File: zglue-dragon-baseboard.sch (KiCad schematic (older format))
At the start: 1 part

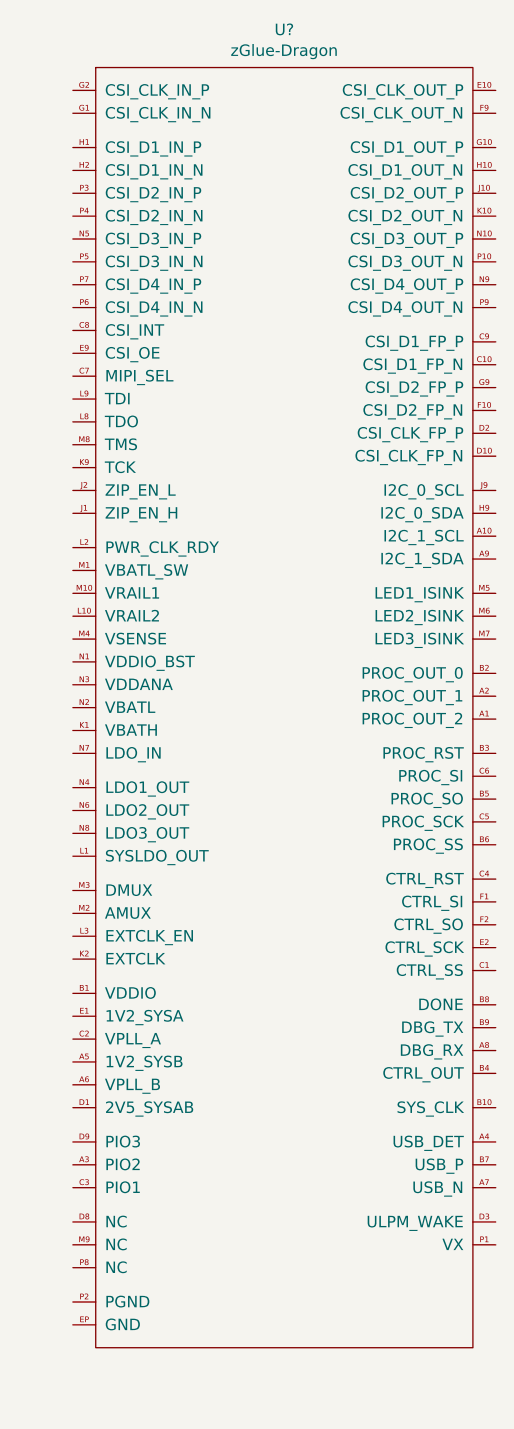
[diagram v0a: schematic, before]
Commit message: Added .gitignore
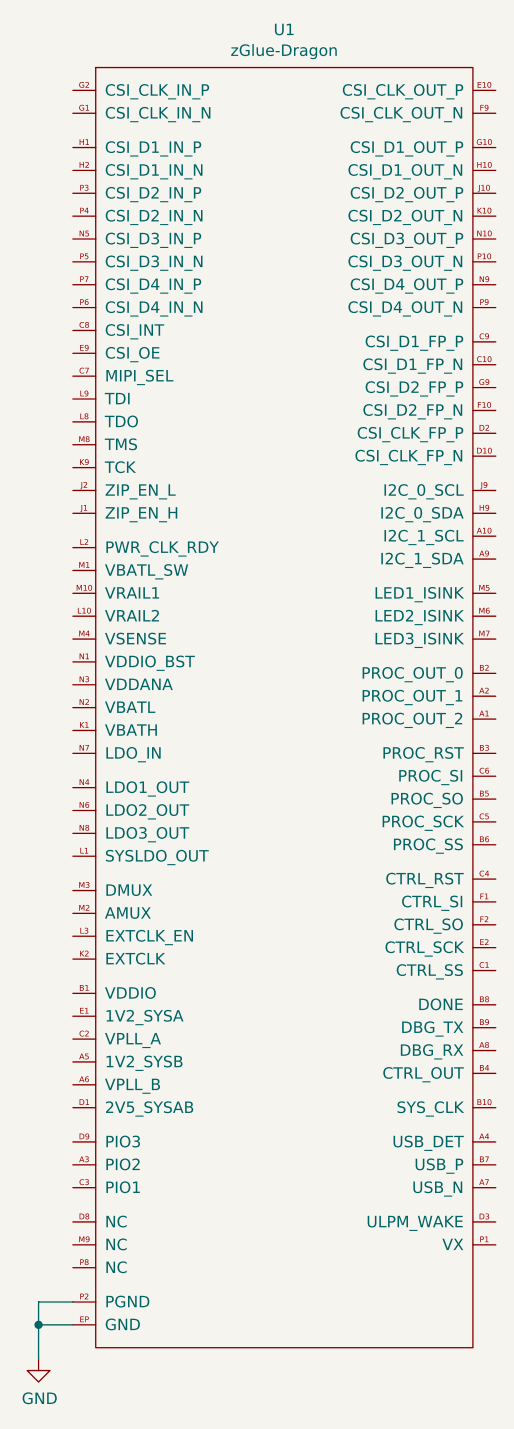
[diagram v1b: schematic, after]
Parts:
- U1: renamed from U?; footprint (none) -> lib:Z-Glue_LGA-96
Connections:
- net GND: now reaches U1.EP (GND)
- net GND: now also U1.P2 (PGND)
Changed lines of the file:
@@
 $EndDescr
 $Comp
-L zglue-dragon:zGlue-Dragon U?
+L zglue-dragon:zGlue-Dragon U1
 U 1 1 5D8CB9E8
 P 3750 3750
-F 0 "U?" H 3825 6165 50  0000 C CNN
+F 0 "U1" H 3825 6165 50  0000 C CNN
 F 1 "zGlue-Dragon" H 3825 6074 50  0000 C CNN
-F 2 "" H 3750 3750 50  0001 C CNN
+F 2 "lib:Z-Glue_LGA-96" H 3750 3750 50  0001 C CNN
 F 3 "" H 3750 3750 50  0001 C CNN
 	1    3750 3750
 	1    0    0    -1
 $EndComp
+$Comp
+L power:GND #PWR?
+U 1 1 5D8CBDC6
+P 2750 7150
+F 0 "#PWR?" H 2750 6900 50  0001 C CNN
+F 1 "GND" H 2755 6977 50  0000 C CNN
+F 2 "" H 2750 7150 50  0001 C CNN
+F 3 "" H 2750 7150 50  0001 C CNN
+	1    2750 7150
+	1    0    0    -1
+$EndComp
+Wire Wire Line
+	2900 6900 2750 6900
+Wire Wire Line
+	2750 6900 2750 7000
+Wire Wire Line
+	2900 7000 2750 7000
+Connection ~ 2750 7000
+Wire Wire Line
+	2750 7000 2750 7150
 $EndSCHEMATC

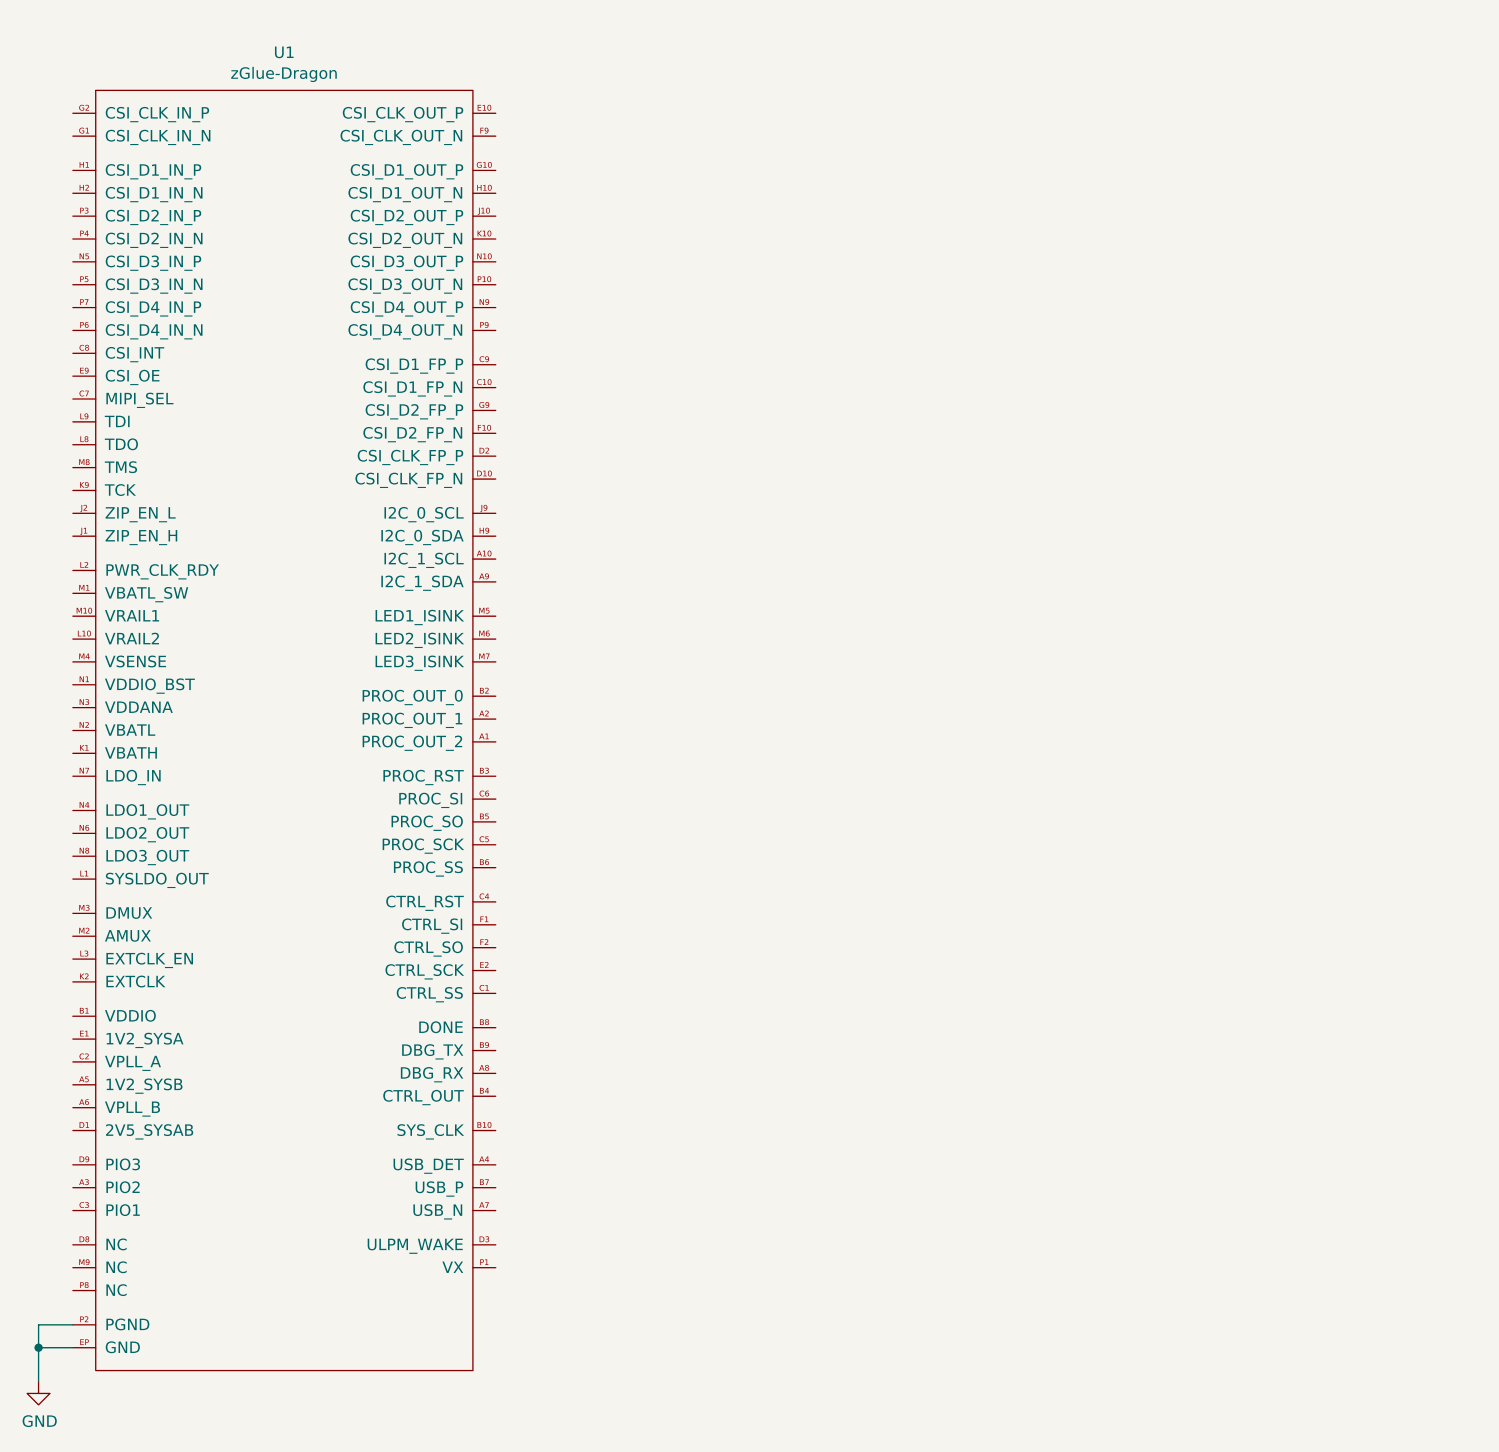
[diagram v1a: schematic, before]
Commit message: Added CSI signals
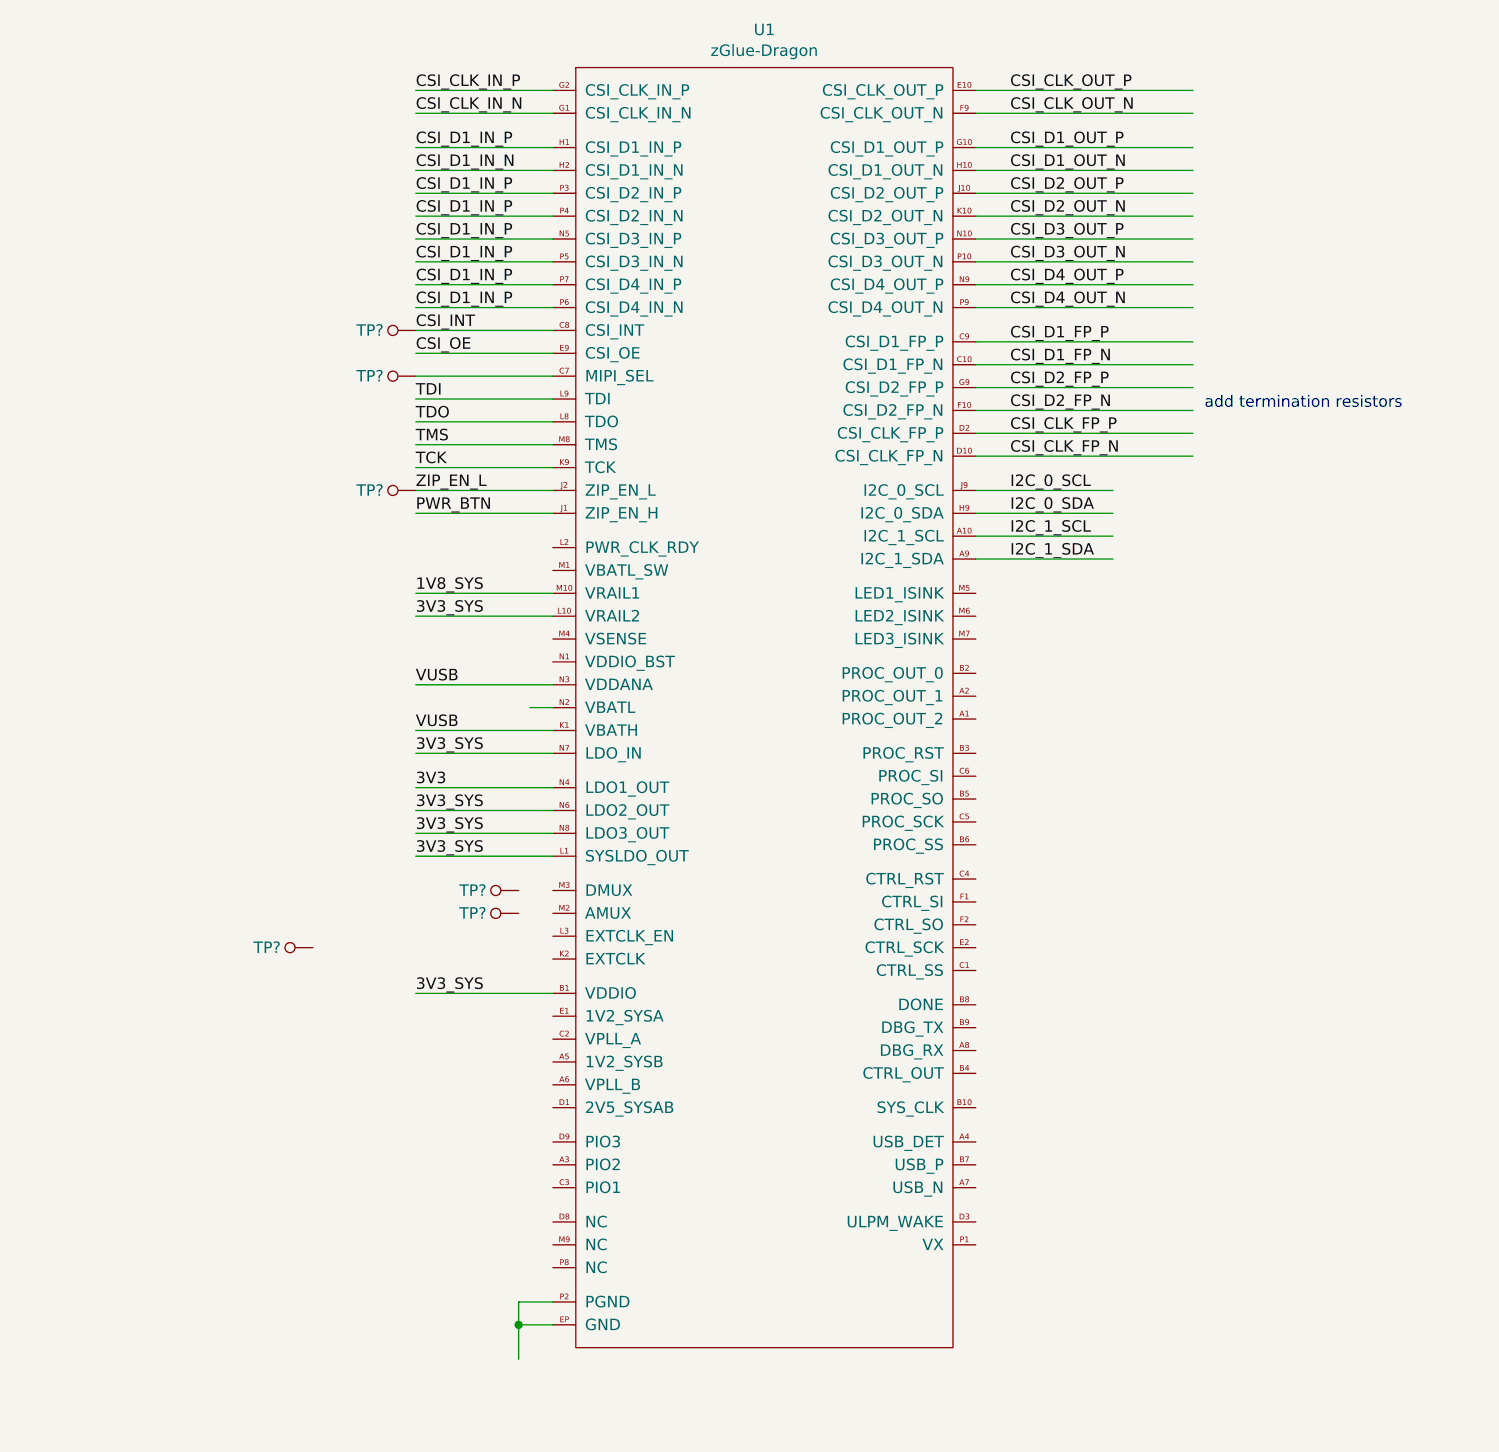
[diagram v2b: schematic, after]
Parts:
- added TP? (x6): TP_SMD1MM, antmicro-footprints:Testpoint_smd_1mm, symbol antmicroTestPoints:TP_SMD1MM
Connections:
- net labels added: 1V8_SYS, 3V3, 3V3_SYS, CSI_CLK_FP_N, CSI_CLK_FP_P, CSI_CLK_IN_N, CSI_CLK_IN_P, CSI_CLK_OUT_N, CSI_CLK_OUT_P, CSI_D1_FP_N, CSI_D1_FP_P, CSI_D1_IN_N, CSI_D1_IN_P, CSI_D1_OUT_N, CSI_D1_OUT_P, CSI_D2_FP_N, CSI_D2_FP_P, CSI_D2_OUT_N, CSI_D2_OUT_P, CSI_D3_OUT_N, CSI_D3_OUT_P, CSI_D4_OUT_N, CSI_D4_OUT_P, CSI_INT, CSI_OE, I2C_0_SCL, I2C_0_SDA, I2C_1_SCL, I2C_1_SDA, PWR_BTN, TCK, TDI, TDO, TMS, VUSB, ZIP_EN_L
- net labels removed: GND
- wire segments 4 -> 54
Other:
- note added: "add termination resistors"
- moved on the sheet: U1
